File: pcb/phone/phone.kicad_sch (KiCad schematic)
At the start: 49 parts, among them CN1 S2B-PH-SM4-TB, U1 STM32H743ZIT6, U4 TPS63021DSJR, U5 TPS7A0218PDBVR, U6 MCP73831-2ACI/MC, U7 MAX17048G+T10, Y1 ECS-80-12-33Q-GN-TR

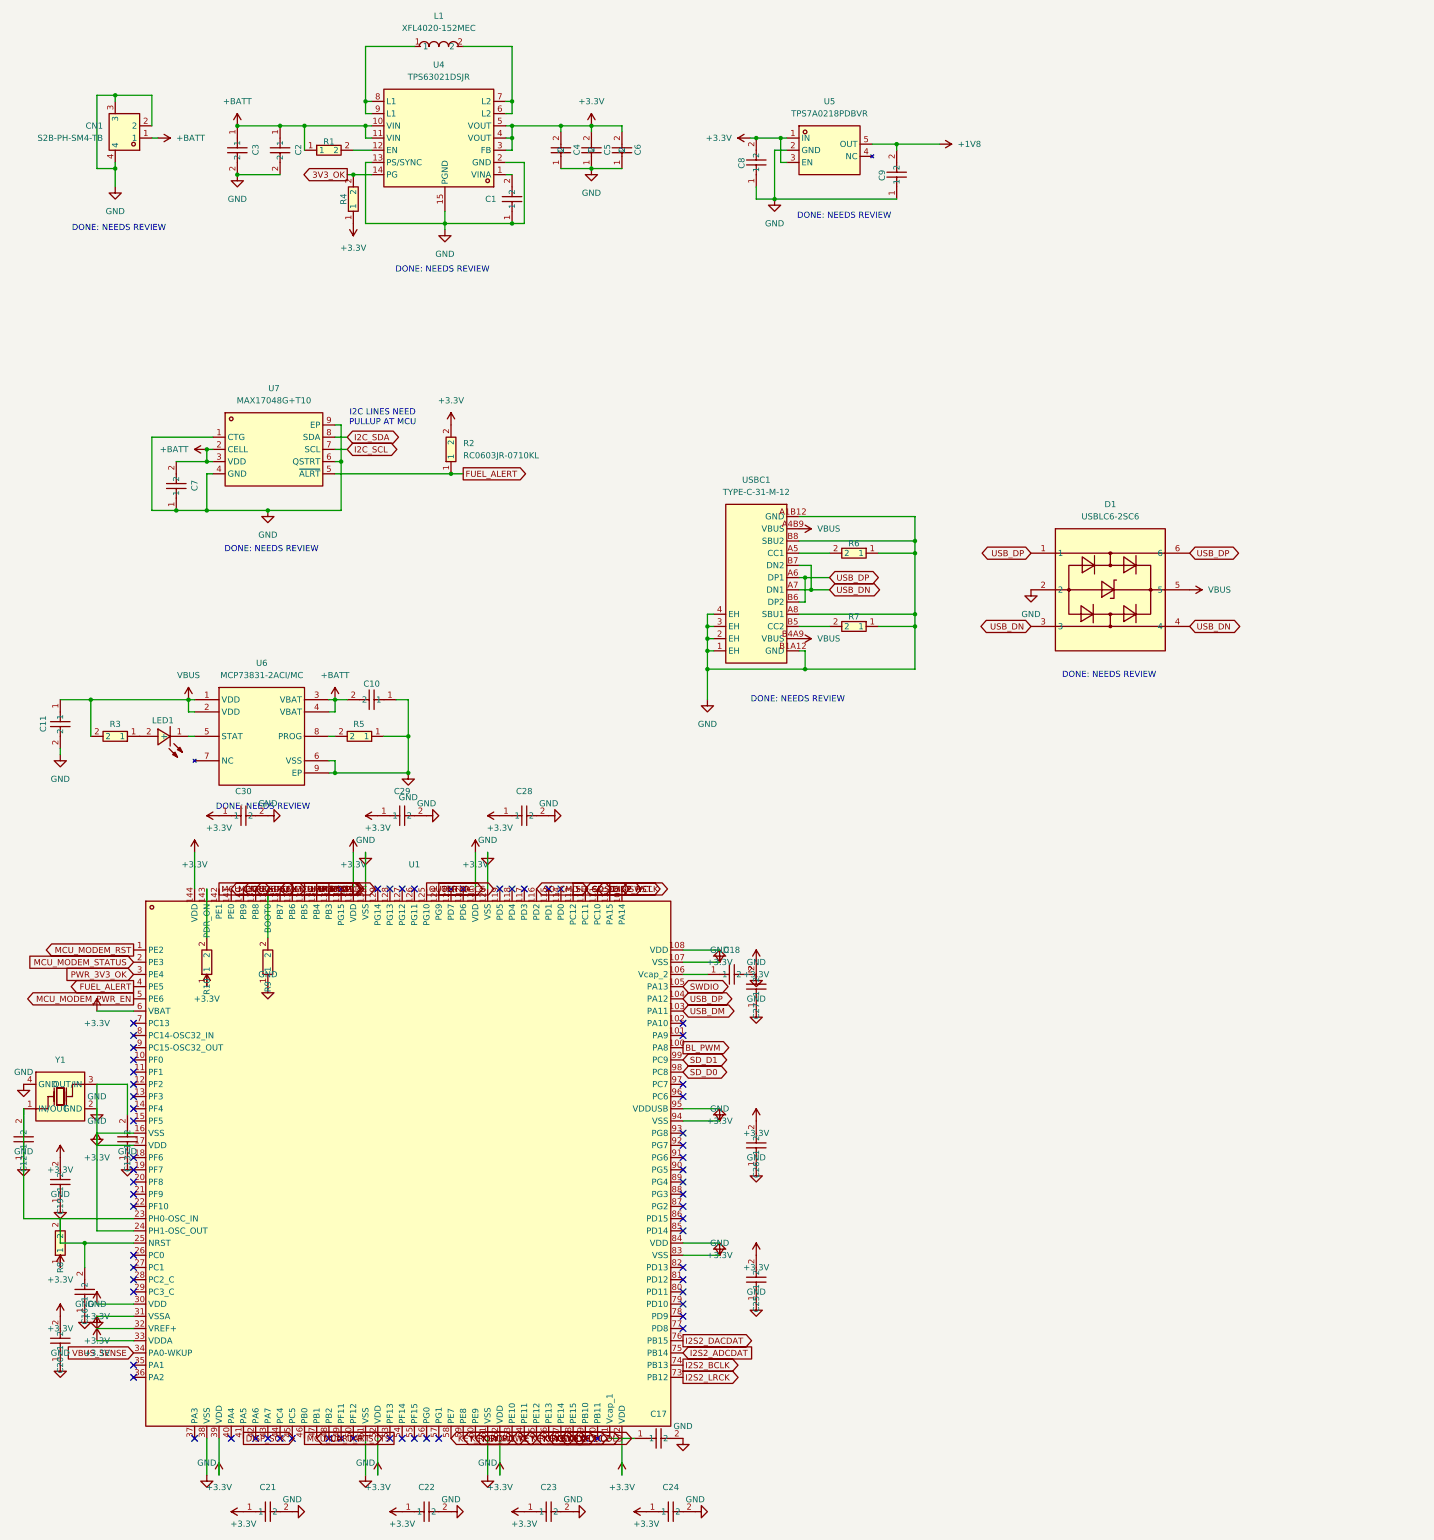
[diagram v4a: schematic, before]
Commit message: Phase 3.2 restructure: Split MCU into hierarchical sheet
- Extract MCU section (STM32H743ZIT6 + decoupling + crystal) from root
  schematic into separate mcu.kicad_sch child sheet
- Root phone.kicad_sch now contains only power section + hierarchical
  sheet box pointing to mcu.kicad_sch
- Fixed label name conflicts: USB_DM -> USB_DN, PWR_3V3_OK -> 3V3_OK
  (to match power section canonical names)
- Normalized lib_symbol indentation (subagent had inserted STM32/crystal
  at 4-tab instead of 2-tab)
- Global labels kept (not converted to hierarchical labels) for cross-
  sheet connectivity without sheet pins
- ERC: 5 pre-existing power errors, 41 warnings (39 isolated pins
  expected + 2 lib_symbol_mismatch cosmetic)

Generated with [Devin](https://devin.ai)

Co-Authored-By: Devin <158243242+devin-ai-integration[bot]@users.noreply.github.com>
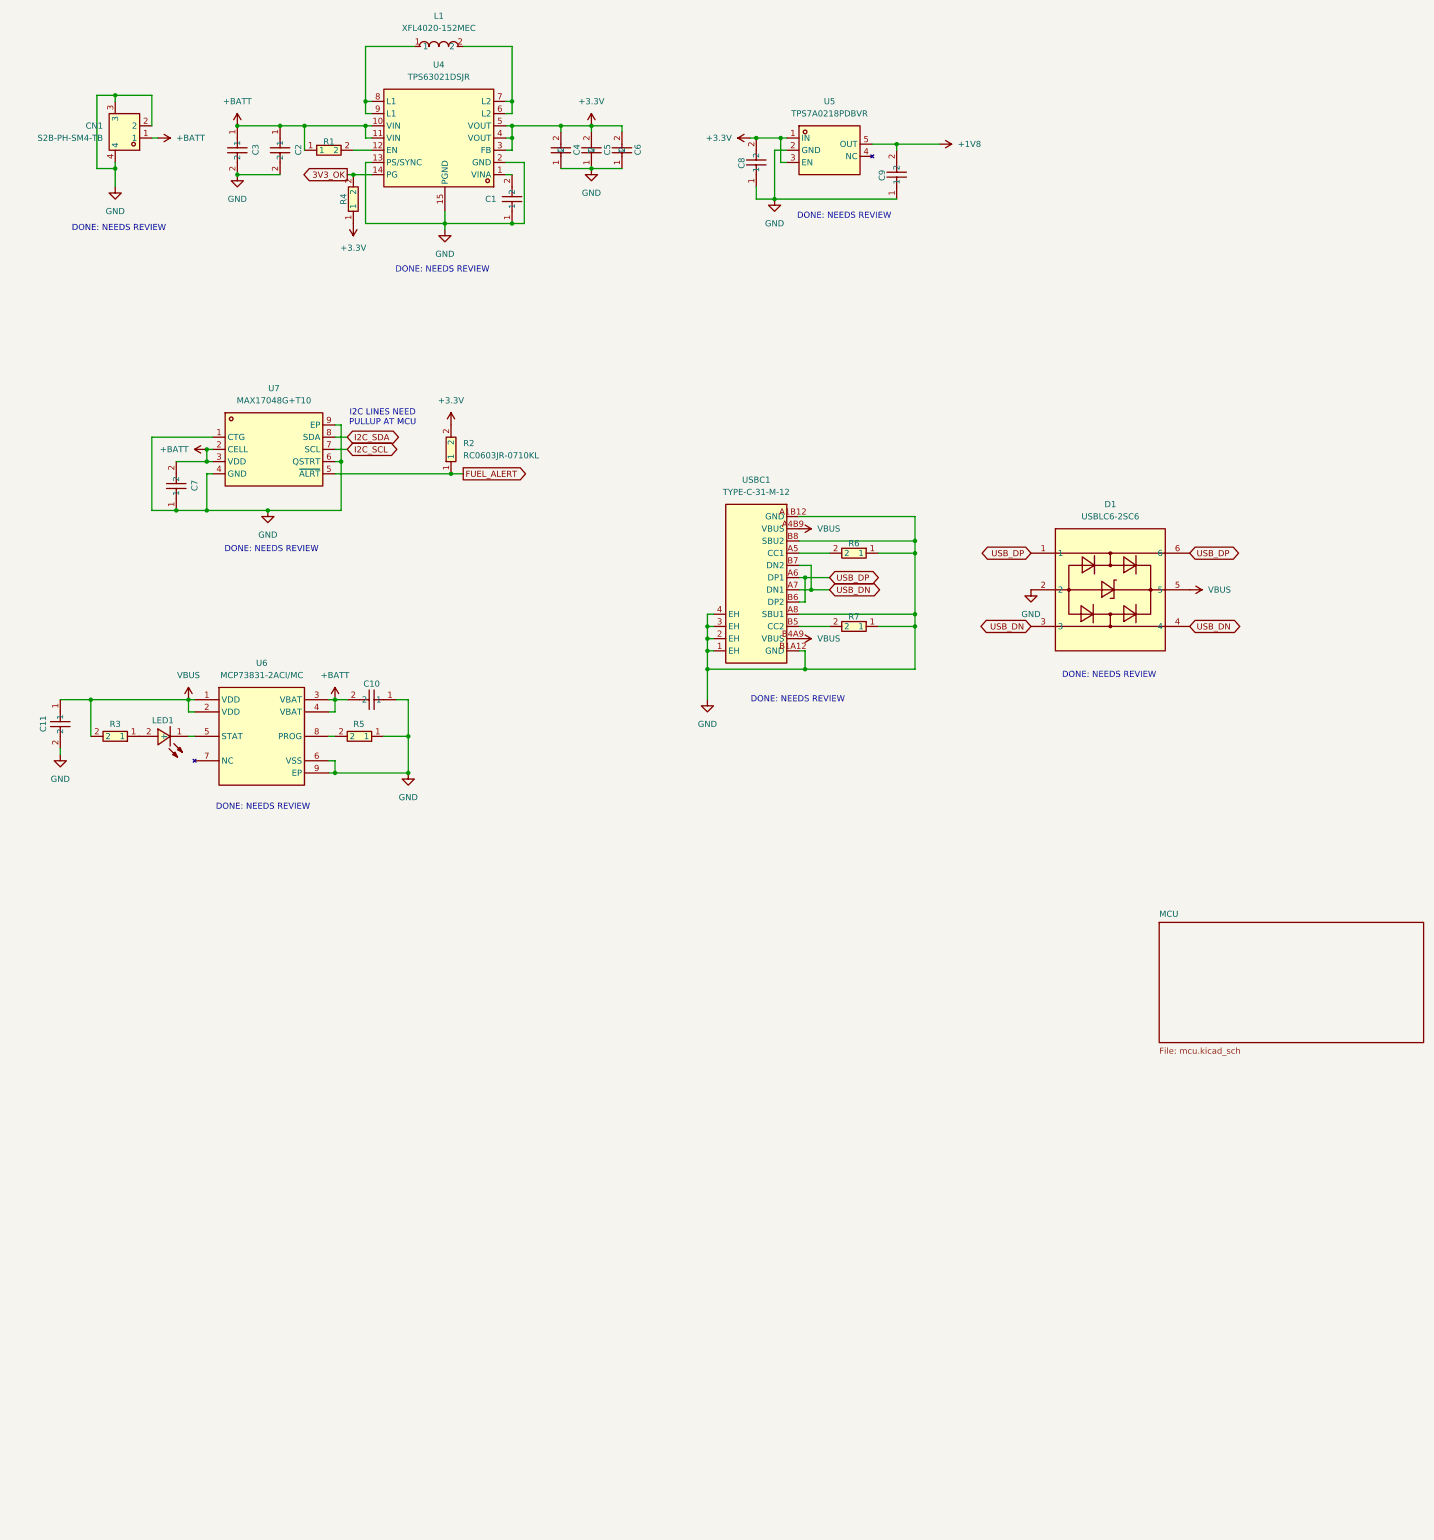
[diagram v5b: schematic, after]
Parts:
- removed C12, C13: 22pF, easyeda2kicad:C0603, symbol passives:CC0603KRX7R9BB104
- removed C16, C19, C20, C21, C22, C23, C24, C25, C26, C27, C28, C29, C30: 100nF, easyeda2kicad:C0603, symbol passives:CC0603KRX7R9BB104
- removed C17, C18: 2.2uF, easyeda2kicad:C0603, symbol passives:GRM188R61C475KE11D
- removed R10, R8, R9: 10k, easyeda2kicad:C0603, symbol passives:RC0603JR-0710KL
- removed U1: STM32H743ZIT6, easyeda2kicad:LQFP-144_L20.0-W20.0-P0.50-LS22.0-BL, symbol ics:STM32H743ZIT6
- removed Y1: ECS-80-12-33Q-GN-TR, easyeda2kicad:CRYSTAL-SMD_4P-L3.2-W2.5-BL, symbol electromech:ECS-80-12-33Q-GN-TR
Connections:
- no-connect marks 67 -> 0
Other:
- added sheet MCU (mcu.kicad_sch)
